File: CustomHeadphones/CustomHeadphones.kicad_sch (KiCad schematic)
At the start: 1 part

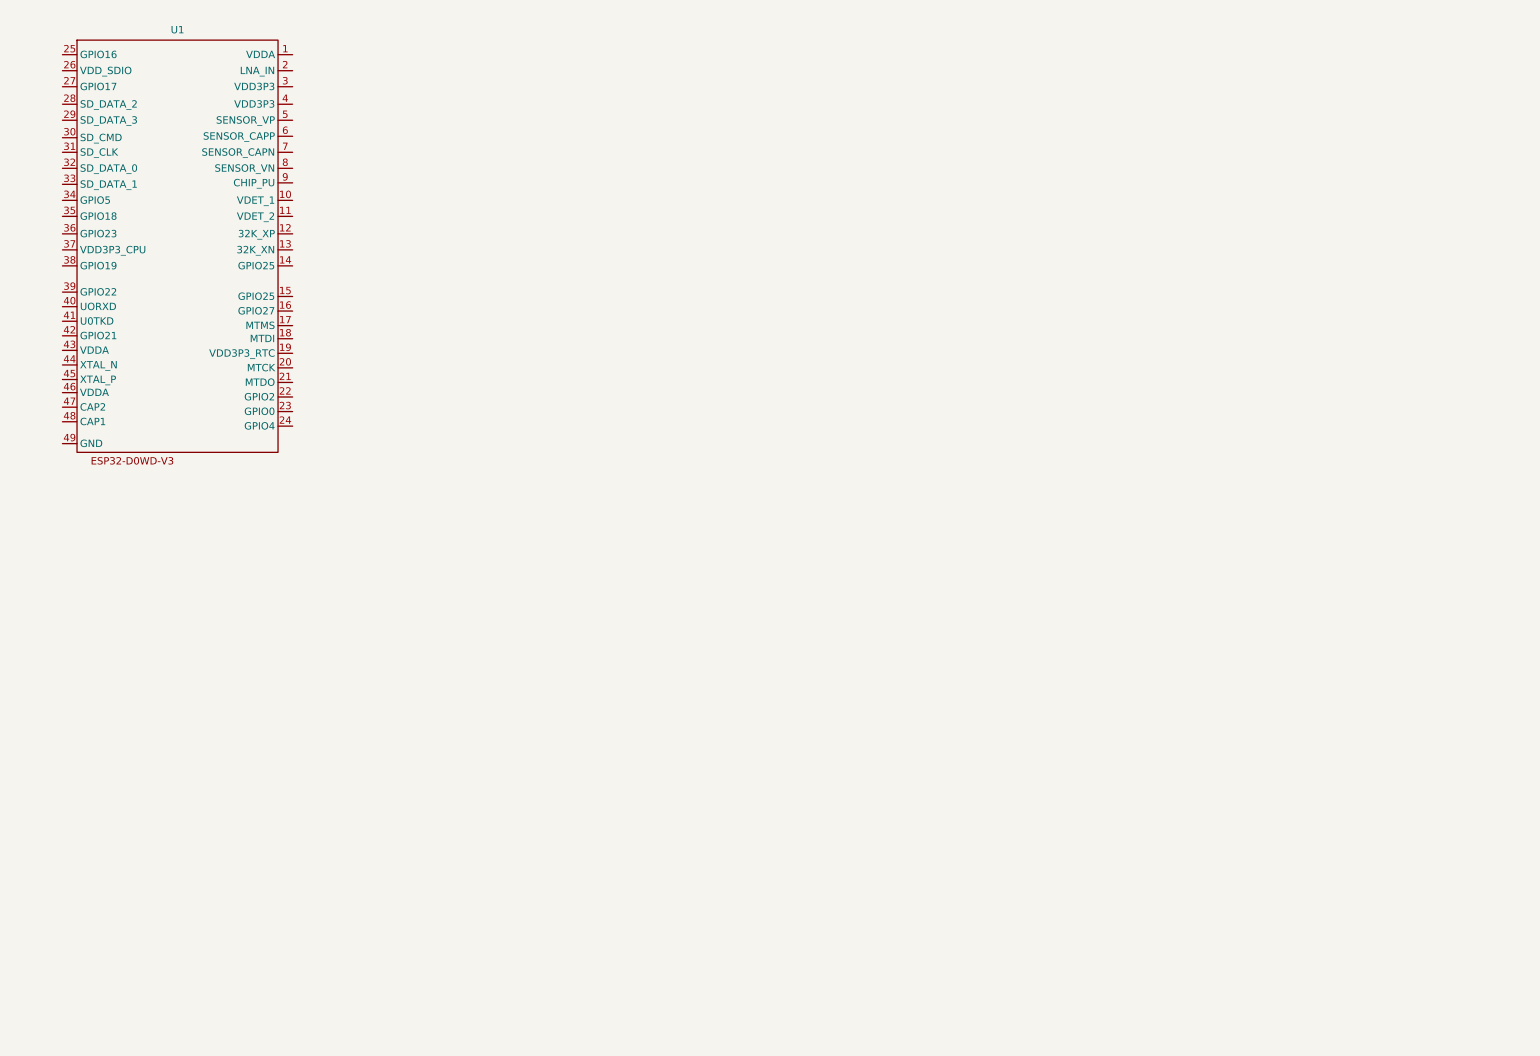
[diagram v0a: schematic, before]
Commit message: Init of codec circuitry, very early power delivery work
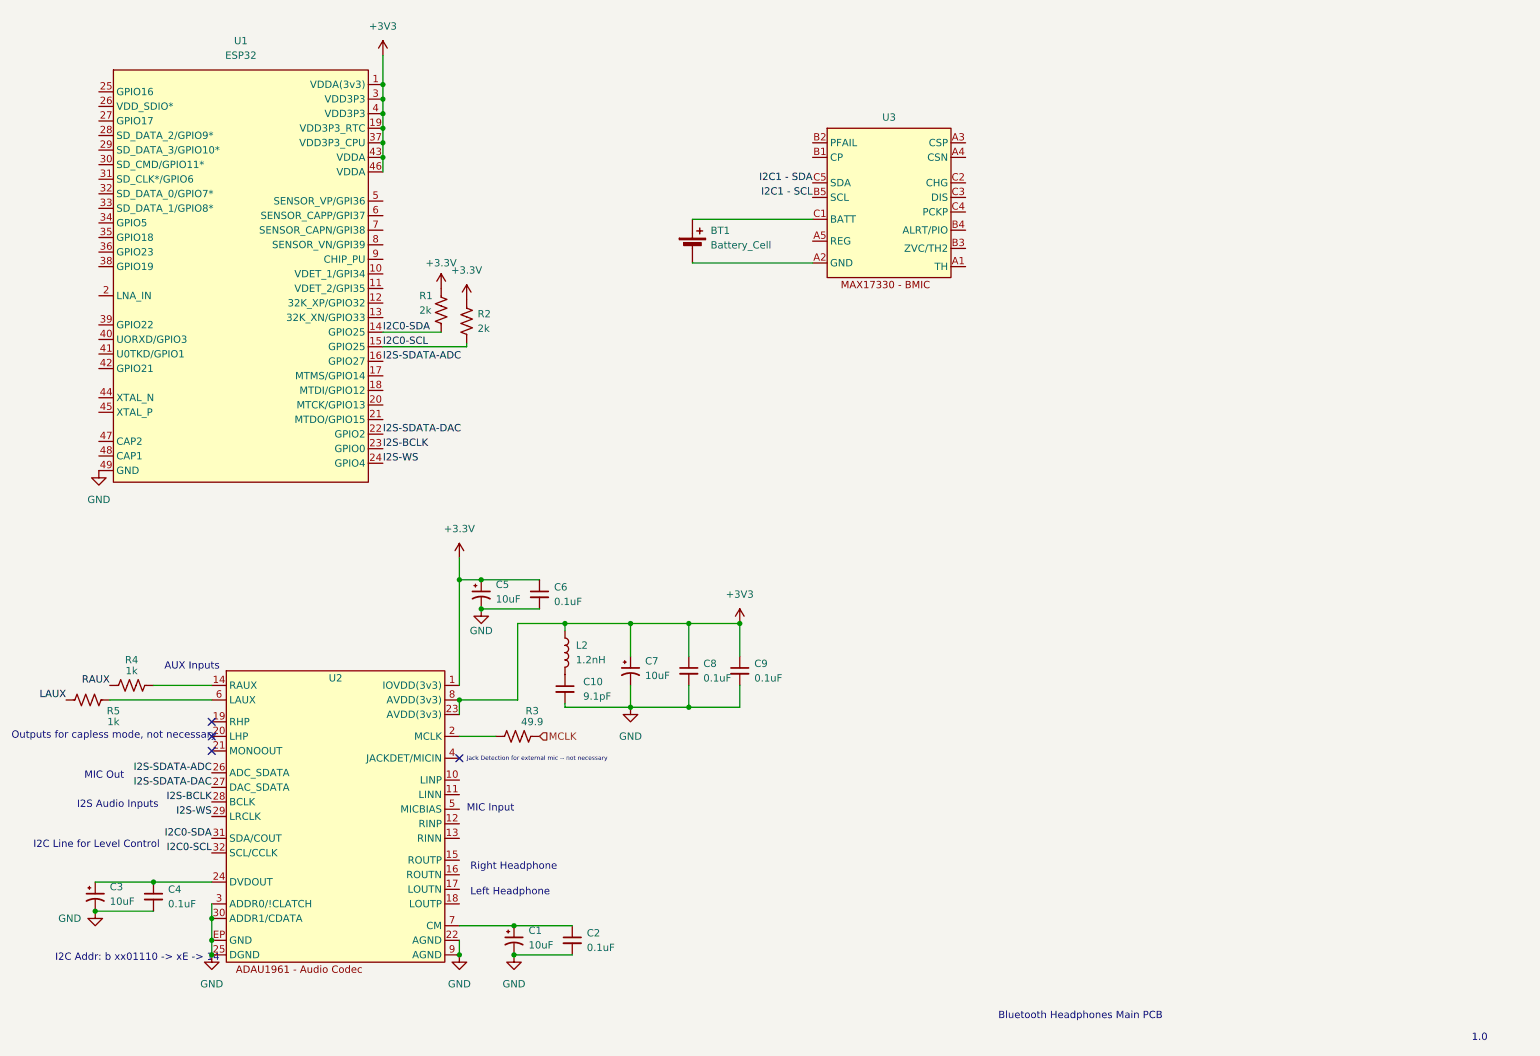
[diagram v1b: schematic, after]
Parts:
- removed U1: ~, symbol CustomSymbols:ESP32-D0WD-V3
- added BT1: Battery_Cell, symbol Device:Battery_Cell
- added C1, C3, C5, C7: 10uF, symbol Device:C_Polarized_Small_US
- added C10: 9.1pF, symbol Device:C_Small
- added C2, C4, C6, C8, C9: 0.1uF, symbol Device:C_Small
- added L2: 1.2nH, symbol Device:L
- added R1, R2: 2k, symbol Device:R_US
- added R3: 49.9, symbol Device:R_US
- added R4, R5: 1k, symbol Device:R_US
- added U1: ESP32, symbol CustomSymbols:ESP32
- added U2: ~, symbol CustomSymbols:ADAU1961
- added U3: ~, symbol CustomSymbols:MAX17330
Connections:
- new net: R4.2, U2.14 (RAUX)
- new net: R3.2, U2.2 (MCLK)
- new net: C3.1, C4.1, U2.24 (DVDOUT)
- new net: R5.2, U2.6 (LAUX)
- new net: C1.1, C2.1, U2.7 (CM)
- new net: BT1.1 (+), U3.C1 (BATT)
- new net: BT1.2 (-), U3.A2 (GND)
- new net: C10.1, L2.2
- new net +3.3V: C5.1, C6.1, R1.1, R2.1, U2.1 (IOVDD(3v3))
- new net +3V3: C7.1, C8.1, C9.1, L2.1, U1.1 (VDDA(3v3)), U1.19 (VDD3P3_RTC), U1.3 (VDD3P3), U1.37 (VDD3P3_CPU), U1.4 (VDD3P3), U1.43 (VDDA), U1.46 (VDDA), U2.23 (AVDD(3v3)), U2.8 (AVDD(3v3))
- new net GND: C1.2, C10.2, C2.2, C3.2, C4.2, C5.2, C6.2, C7.2, C8.2, C9.2, U1.49 (GND), U2.22 (AGND), U2.25 (DGND), U2.3 (ADDR0/!CLATCH), U2.30 (ADDR1/CDATA), U2.9 (AGND), U2.EP (GND)
- new net I2C0-SCL: R2.2, U1.15 (GPIO25), U2.32 (SCL/CCLK)
- new net I2C0-SDA: R1.2, U1.14 (GPIO25), U2.31 (SDA/COUT)
- new net I2C1 - SCL: U3.B5 (SCL)
- new net I2C1 - SDA: U3.C5 (SDA)
- new net I2S-BCLK: U1.23 (GPIO0), U2.28 (BCLK)
- new net I2S-SDATA-ADC: U1.16 (GPIO27), U2.26 (ADC_SDATA)
- new net I2S-SDATA-DAC: U1.22 (GPIO2), U2.27 (DAC_SDATA)
- new net I2S-WS: U1.24 (GPIO4), U2.29 (LRCLK)
- new net LAUX: R5.1
- new net MCLK: R3.1
- new net RAUX: R4.1
- no-connect marks 0 -> 4
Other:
- note added: "1.0"
- note added: "AUX Inputs"
- note added: "Bluetooth Headphones Main PCB"
- note added: "I2C Addr: b xx01110 -> xE -> 14"
- note added: "I2C Line for Level Control"
- note added: "I2S Audio Inputs"
- note added: "Jack Detection for external mic -- not necessary"
- note added: "Left Headphone"
- note added: "MIC Input"
- note added: "MIC Out"
- note added: "Outputs for capless mode, not necessary"
- note added: "Right Headphone"

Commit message: MAX17330 Circuit 95% complete
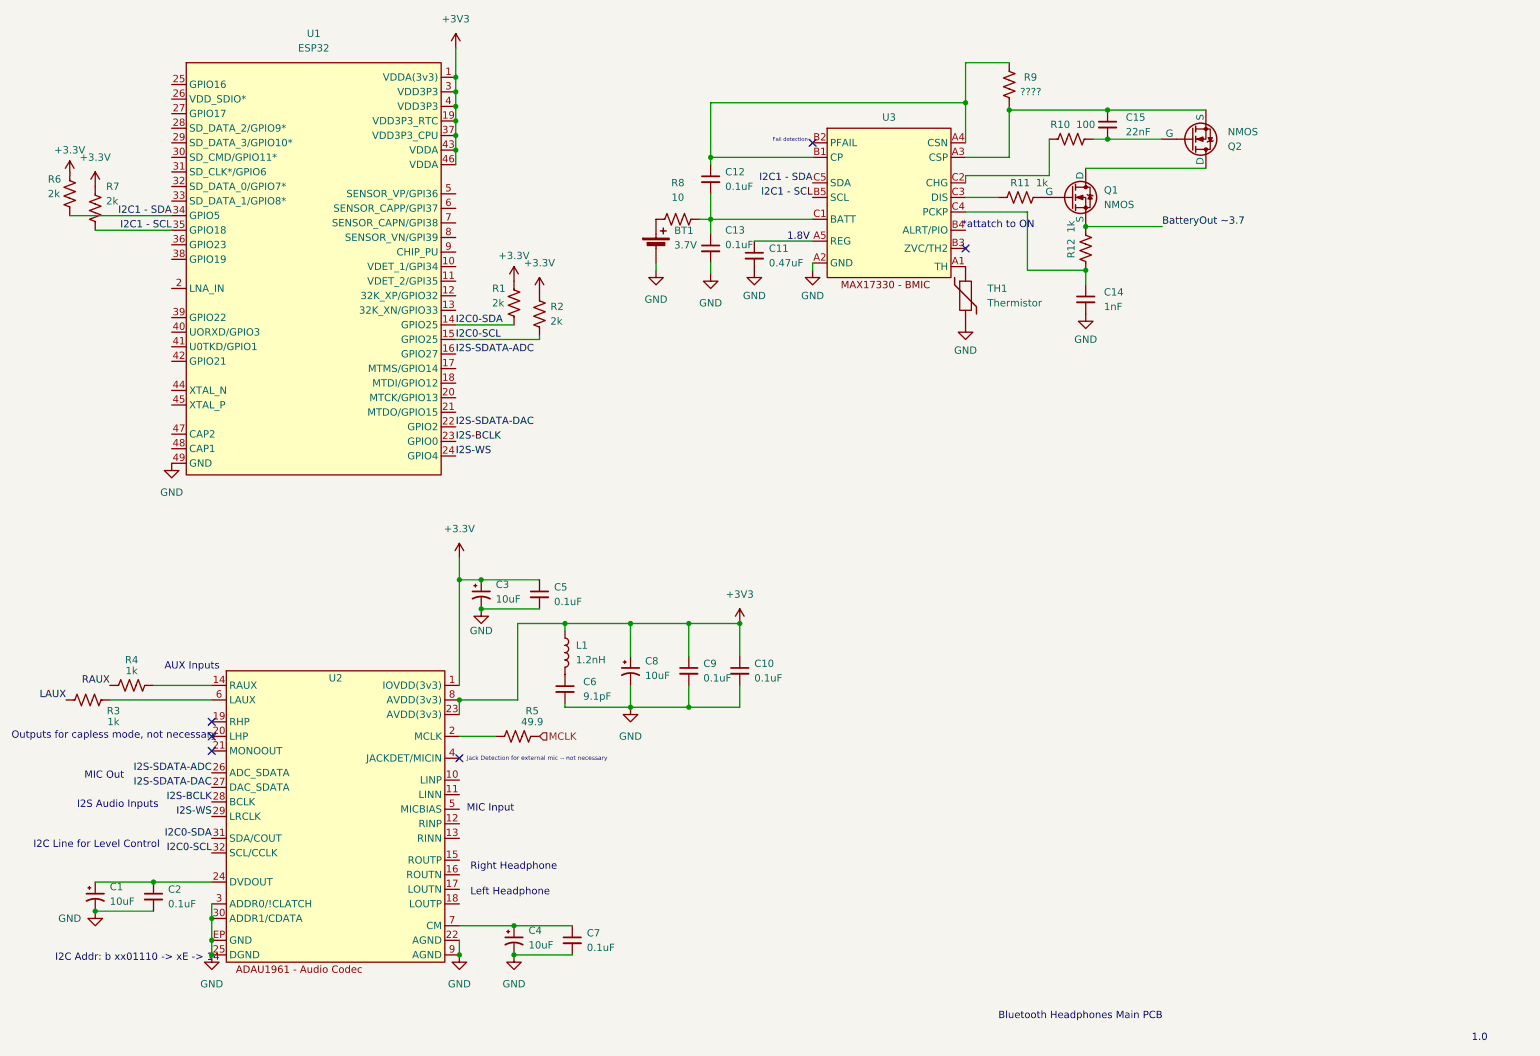
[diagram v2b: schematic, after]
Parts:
- added C11: 0.47uF, symbol Device:C_Small
- added C12, C13: 0.1uF, symbol Device:C_Small
- added C14: 1nF, symbol Device:C_Small
- added C15: 22nF, symbol Device:C_Small
- added Q1, Q2: NMOS, symbol Simulation_SPICE:NMOS
- added R10: 100, symbol Device:R_US
- added R11, R12: 1k, symbol Device:R_US
- added R6, R7: 2k, symbol Device:R_US
- added R8: 10, symbol Device:R_US
- added R9: ????, symbol Device:R_US
- added TH1: Thermistor, symbol Device:Thermistor
- BT1: value Battery_Cell -> 3.7V
- renumbered C3 to C1, C9 to C10, C4 to C2, C5 to C3, C1 to C4, C6 to C5, C10 to C6, C2 to C7, C7 to C8, C8 to C9, L2 to L1, R5 to R3, R3 to R5
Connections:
- net +3.3V: now also R6.1, R7.1
- net GND: now also BT1.2 (-), U3.A2 (GND), C11.2, C13.2, C14.2, TH1.2
- net I2C1 - SCL: now also U1.35 (GPIO18), R7.2
- net I2C1 - SDA: now also U1.34 (GPIO5), R6.2
- net at U3.C1 (BATT): now also C12.2, C13.1, R8.2; no longer BT1.1 (+)
- net at U3.A1 (TH): now also TH1.1
- net at U3.A3 (CSP): now also C15.1, Q2.3 (S), R9.1
- net at U3.A4 (CSN): now also U3.B1 (CP), C12.1, R9.2
- net at U3.A5 (REG): now also C11.1
- net at U3.C2 (CHG): now also R10.1
- net at U3.C3 (DIS): now also R11.1
- net at U3.C4 (PCKP): now also C14.1, R12.1
- new net: Q1.1 (D), Q2.1 (D)
- new net: Q1.2 (G), R11.2
- new net: BT1.1 (+), R8.1
- new net: C15.2, Q2.2 (G), R10.2
- new net BatteryOut ~3.7: Q1.3 (S), R12.2
- no-connect marks 4 -> 6
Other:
- note added: "*attatch to ON"
- note added: "1.8V"
- note added: "Fail detection"
- moved on the sheet: BT1, R1, R2, U1

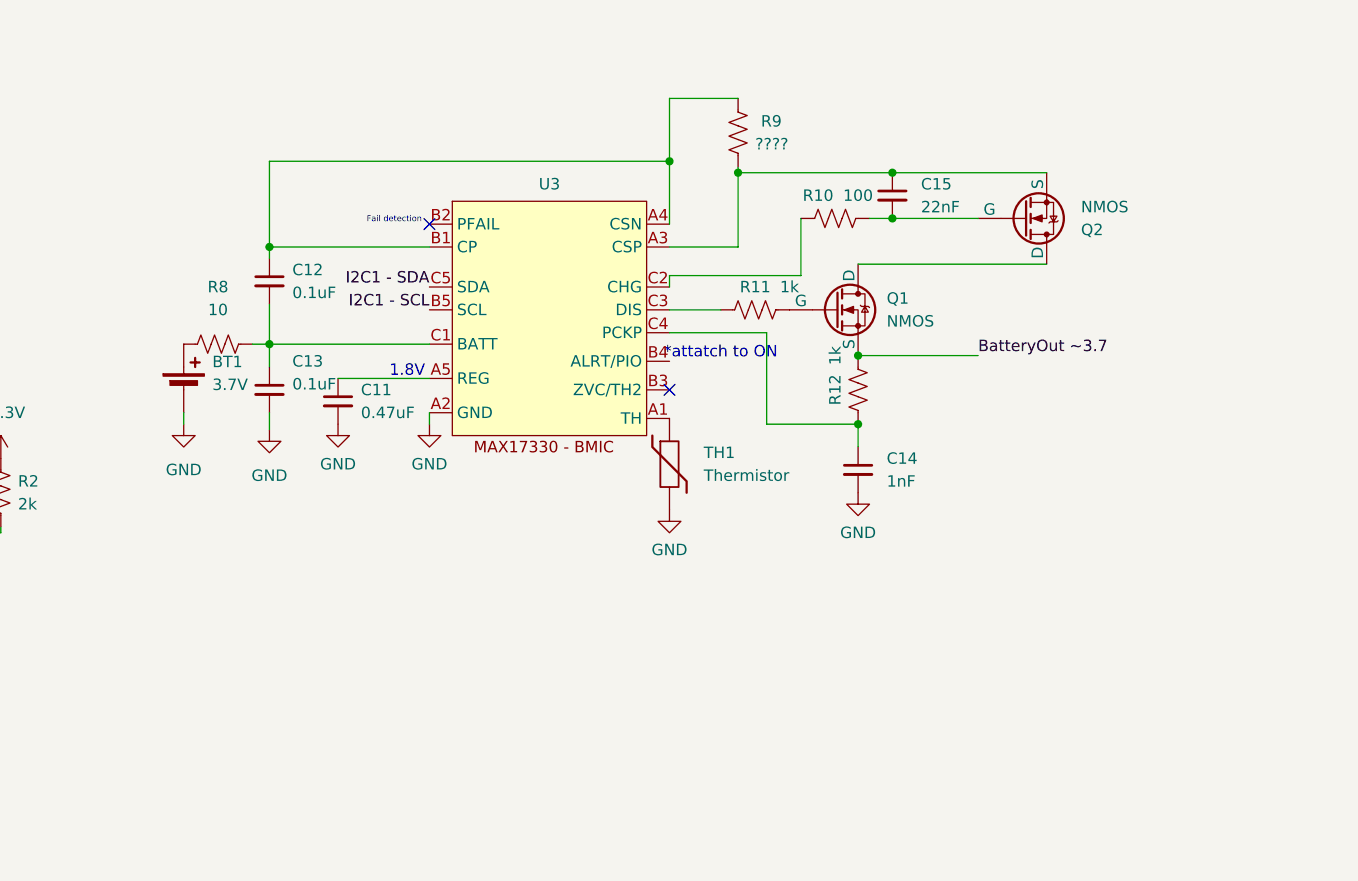
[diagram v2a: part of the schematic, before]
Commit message: LDO circuitry and USB connector symbol
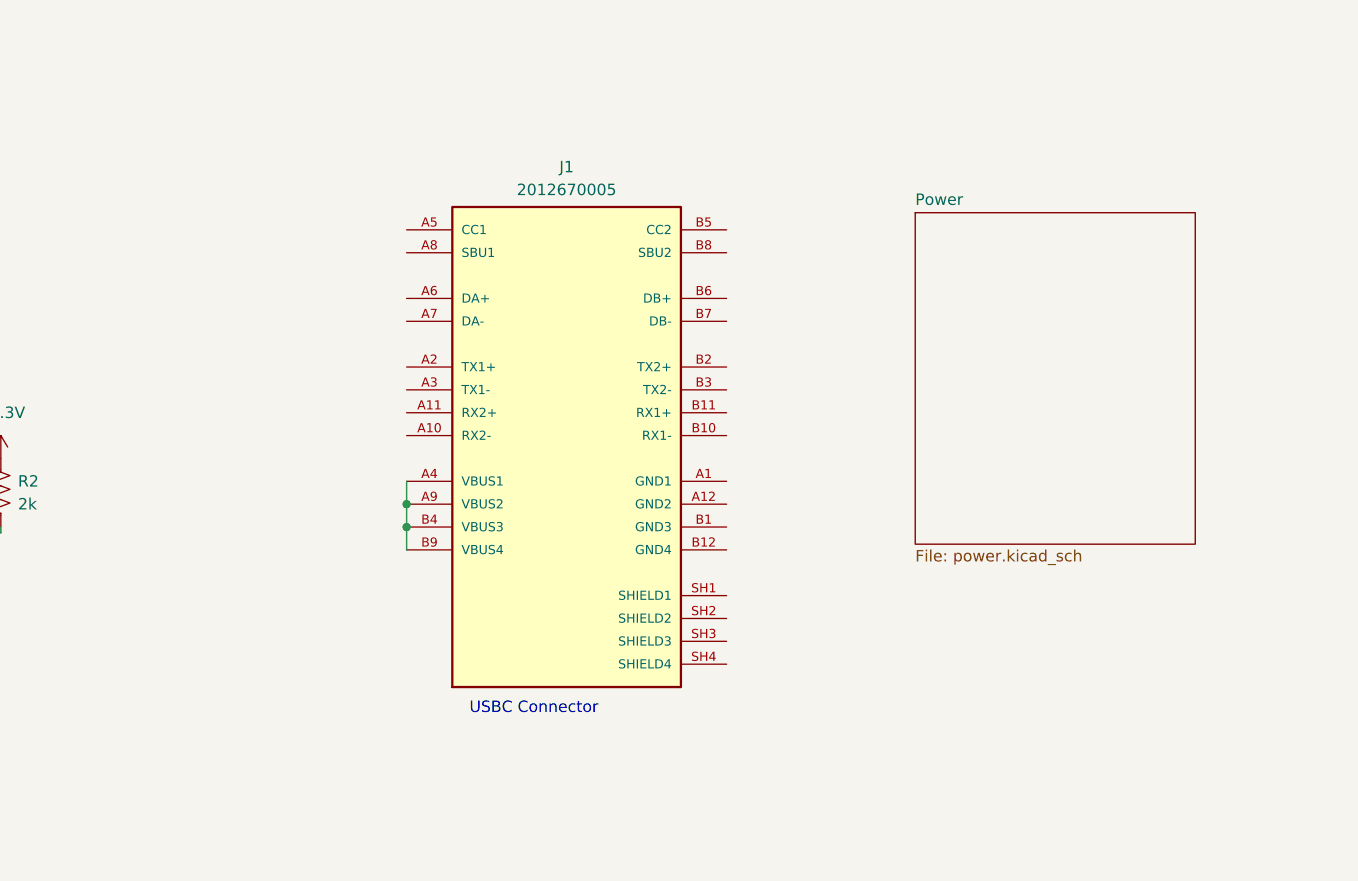
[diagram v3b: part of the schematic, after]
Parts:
- removed BT1: 3.7V, symbol Device:Battery_Cell
- removed C11: 0.47uF, symbol Device:C_Small
- removed C12, C13: 0.1uF, symbol Device:C_Small
- removed C14: 1nF, symbol Device:C_Small
- removed C15: 22nF, symbol Device:C_Small
- removed Q1, Q2: NMOS, symbol Simulation_SPICE:NMOS
- removed R10: 100, symbol Device:R_US
- removed R11, R12: 1k, symbol Device:R_US
- removed R8: 10, symbol Device:R_US
- removed R9: ????, symbol Device:R_US
- removed TH1: Thermistor, symbol Device:Thermistor
- removed U3: ~, symbol CustomSymbols:MAX17330
- added J1: 2012670005, 2012670005:MOLEX_2012670005, symbol 2012670005:2012670005
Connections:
- new net: J1.A4 (VBUS1), J1.A9 (VBUS2), J1.B4 (VBUS3), J1.B9 (VBUS4)
- no-connect marks 6 -> 4
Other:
- added sheet Power (power.kicad_sch)
- note added: "USBC Connector"
- note removed: "*attatch to ON"
- note removed: "1.8V"
- note removed: "Fail detection"

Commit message: sync, more work on charging
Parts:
- added C17: 10uF, symbol Device:C_Small
- added D1: D_Schottky, symbol Device:D_Schottky
- added D2: LED, symbol Device:LED
- added Q3, Q4: NMOS, symbol Simulation_SPICE:NMOS
- added R13: 10k, symbol Device:R_US
- added R15: SPEC FOR LED, symbol Device:R_US
- added U5: CP2102N-A02-GQFN28R, CP2102N-A02-GQFN28R:IC_CP2102N-A02-GQFN28R, symbol CP2102N-A02-GQFN28R:CP2102N-A02-GQFN28R
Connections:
- net +3.3V: now also R13.1
- net +3V3: now also C17.1, U5.6 (VDD), U5.7 (VREGIN), U5.9 (~{RST})
- net GND: now also C17.2, R15.2, U5.11 (~{SUSPEND}), U5.29 (EXP), U5.3 (GND)
- net I2S-BCLK: no longer U1.23 (GPIO0)
- net I2S-SDATA-DAC: no longer U1.22 (GPIO2)
- net I2S-WS: no longer U1.24 (GPIO4)
- net CHIP_PU: now reaches U1.9 (CHIP_PU)
- net CHIP_PU: now also Q3.1 (D), R13.2
- net VBUS: now reaches J1.A4 (VBUS1), J1.A9 (VBUS2), J1.B4 (VBUS3), J1.B9 (VBUS4)
- net VBUS: now also D1.2 (A), D2.2 (A), U5.8 (VBUS)
- net USB_D+: now reaches J1.A6 (DA+)
- net USB_D+: now also U5.4 (D+)
- net USB_D-: now reaches J1.A7 (DA-)
- net USB_D-: now also U5.5 (D-)
- net MCLK: no longer names the net of R5.1
- new net: Q3.3 (S), Q4.2 (G), U5.24 (RTS)
- new net: D2.1 (K), R15.1
- new net DTR: Q3.2 (G), Q4.3 (S), U5.28 (DTR)
- new net GPIO0: Q4.1 (D), U1.23 (GPIO0)
- new net UART0_RX: U5.26 (TXD)
- new net UART0_TX: U5.25 (RXD)
- new net Vcharge: D1.1 (K)
- no-connect marks 4 -> 17
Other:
- sheet Power ports: added VPACK; removed none
- note added: "Charge indicator"
- note added: "NEED TO CHECK ALL THIS"
- note added: "NEED TO CONNECT"
- note added: "internal pull up, pull down for download boot"
- note added: "pull down internal"
- note added: "used for bootsel, internal pulldown"
- moved on the sheet: C10, C3, C5, C6, C8, C9, L1, R5
